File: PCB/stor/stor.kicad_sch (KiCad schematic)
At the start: 45 parts, among them J1 Conn_01x04_Socket, SW1 TS1603-TZ38HBM, SW2 TS1603-TZ38HBM, U1 STM32H723VGT6, U2 TYPE-C 24P-GTJB 040, U3 USB3300-EZK-TR, U4 TPS62177DQCR, X1 25mhz, X2 32.768k, X3 24mhz

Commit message: soo much routing
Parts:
- added R10, R11, R7, R8, R9: 10k, easyeda2kicad:R0402, symbol easyeda2kicad:RC0402FR-0710KL
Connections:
- net PC10: now also R10.2
- net PC11: now also R11.2
- net PC12: now also U1.80 (PC12)
- net PC8: now also R7.1
- net PC9: now also R8.1
- net PD2: now also R9.2
- net VDD: now also R10.1, R11.1, R7.2, R8.2, R9.1

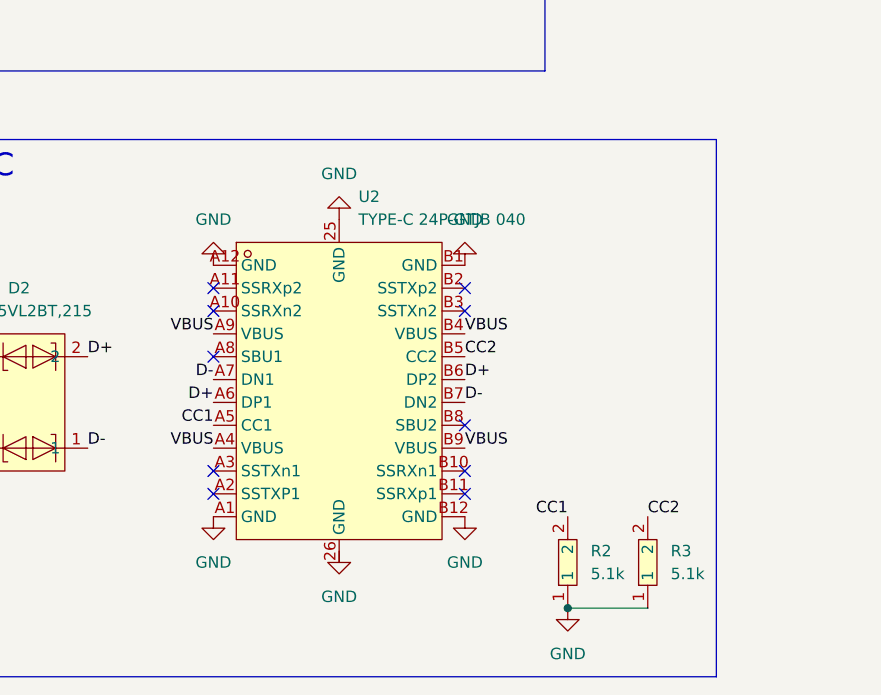
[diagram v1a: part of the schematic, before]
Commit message: new usb and uh finish routing!
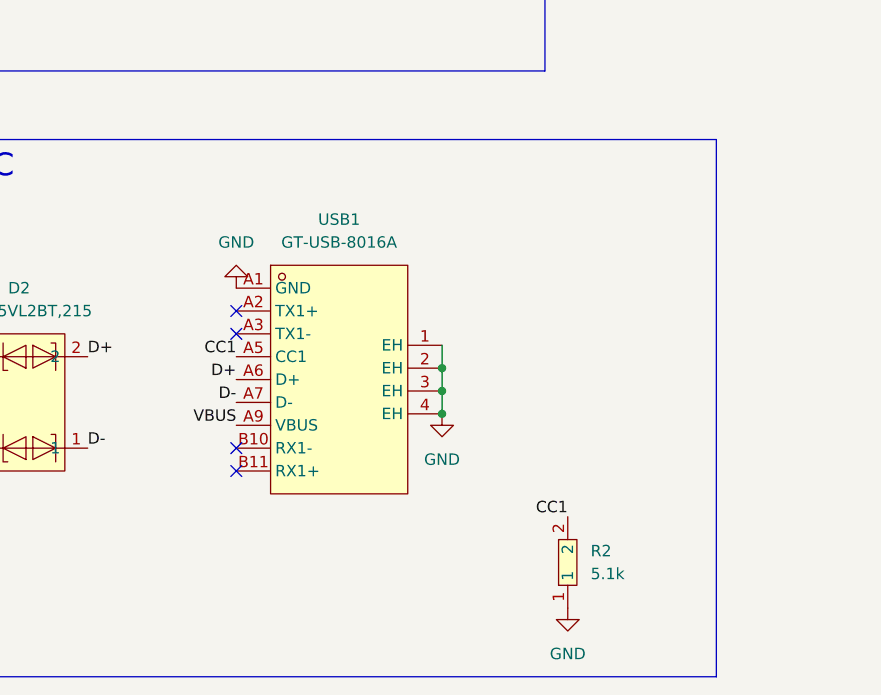
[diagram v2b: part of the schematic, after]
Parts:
- removed R3: 5.1k, easyeda2kicad:R0402, symbol easyeda2kicad:RC0402FR-075K1L
- removed U2: TYPE-C 24P-GTJB 040, easyeda2kicad:USB-C-SMD_TYPE-C-24P-GTJB-040, symbol easyeda2kicad:TYPE-C24P-GTJB040
- added USB1: GT-USB-8016A, easyeda2kicad:USB-TYPE-C-SMD_GT-USB-8016A, symbol easyeda2kicad:GT-USB-8016A
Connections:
- net CC1: now also USB1.A5 (CC1)
- net D+: now also USB1.A6 (D+)
- net D-: now also USB1.A7 (D-)
- net GND: now also USB1.1 (EH), USB1.2 (EH), USB1.3 (EH), USB1.4 (EH), USB1.A1 (GND)
- net VBUS: now also USB1.A9 (VBUS)
- no-connect marks 14 -> 8

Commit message: Reapply "um"
This reverts commit 07b64e62ca9c6bf6512e2ad29080b55d79604863.
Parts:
- removed C11, C12: 10pF, easyeda2kicad:C0402, symbol easyeda2kicad:CC0402JRNPO9BN100
- removed C13, C14: 12pF, easyeda2kicad:C0402, symbol easyeda2kicad:CC0402JRNPO9BN120
- removed C17: 22uF, easyeda2kicad:C0402, symbol easyeda2kicad:GRM158C80G226ME01D
- removed C18: 4.7uF, easyeda2kicad:C0402, symbol easyeda2kicad:CL05A475KP5NRNC
- removed C24, C25: 33pF, easyeda2kicad:C0402, symbol easyeda2kicad:CL05C330JB5NNNC
- removed D2: PESD15VL2BT,215, easyeda2kicad:SOT-23-3_L2.9-W1.3-P1.90-LS2.4-BR, symbol easyeda2kicad:PESD15VL2BT,215
- added C11, C12, C13, C14, C24, C25: 18pF, easyeda2kicad:C0402, symbol lcsc:CC0402JRNPO9BN180
- added C17: 22uF, easyeda2kicad:C0402, symbol lcsc:HGC0402R5226M100NTEJ
- added C18, C27: 100nF, easyeda2kicad:C0402, symbol easyeda2kicad:CC0402KRX7R7BB104
- added C29: 4.7uF, easyeda2kicad:C0402, symbol easyeda2kicad:CL05A475KP5NRNC
- added D1: USBLC6-2SC6, easyeda2kicad:SOT-23-6_L2.9-W1.6-P0.95-LS2.8-BL, symbol lcsc:USBLC6-2SC6
- R6: value 1mΩ -> 1 MΩ
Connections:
- net D+: now also D1.3, D1.4
- net D-: now also D1.1, D1.6
- net GND: now also C11.2, C12.2, C13.2, C14.2, C17.1, C18.1, C24.1, C25.1, C27.1, C29.2, D1.2
- net PC14: now also C13.1
- net PC15: now also C14.1
- net PH0: now also C12.1
- net PH1: now also C11.1
- net VBUS: now also D1.5
- net VDD: now also C21.2, U4.8 (SLEEP), C17.2, C18.2, C27.2, C29.1
- net XI: now also C25.2
- net XO: now also C24.2
- net VDD1.8: now reaches C19.2, U3.15 (VDD1.8)
- net VDD1.8: now also C20.2, U3.26 (VDD1.8)
- no-connect marks 8 -> 7
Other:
- moved on the sheet: R2, USB1

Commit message: zomg
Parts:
- removed J1: Conn_01x04_Socket, Connector_PinHeader_2.54mm:PinHeader_1x04_P2.54mm_Vertical, symbol Connector:Conn_01x04_Socket
- added J1: Conn_01x05_Socket, Connector_PinSocket_2.54mm:PinSocket_1x05_P2.54mm_Vertical, symbol Connector:Conn_01x05_Socket
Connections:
- net GND: now also J1.1 (Pin_1)
- net NRST: now also J1.2 (Pin_2)
- net SWCLK: now also J1.3 (Pin_3)
- net SWDIO: now also J1.4 (Pin_4)
- net VDD: now also J1.5 (Pin_5)
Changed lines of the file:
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@@
 		)
 	)
-	(label "XO"
-		(at 229.87 33.02 180)
+	(label "NRST"
+		(at 24.13 106.68 0)
 		(effects
 			(font
 				(size 1.27 1.27)
 			)
-			(justify right bottom)
+			(justify left bottom)
 		)
 	)
 	(label "XO"
-		(at 251.46 29.21 180)
+		(at 229.87 33.02 180)
 		(effects
 			(font
@@
 		)
 	)
-	(label "SWDIO"
-		(at 35.56 90.17 0)
+	(label "XO"
+		(at 251.46 29.21 180)
 		(effects
 			(font
 				(size 1.27 1.27)
 			)
-			(justify left bottom)
+			(justify right bottom)
 		)
 	)
@@
 		)
 	)
-	(label "VDD"
-		(at 35.56 87.63 0)
-		(effects
-			(font
-				(size 1.27 1.27)
-			)
-			(justify left bottom)
-		)
-	)
 	(label "PB0"
 		(at 251.46 73.66 0)
@@
 		)
 	)
+	(label "SWCLK"
+		(at 24.13 104.14 0)
+		(effects
+			(font
+				(size 1.27 1.27)
+			)
+			(justify left bottom)
+		)
+	)
 	(label "VDD"
 		(at 100.33 189.23 0)
@@
 		)
 	)
+	(label "SWDIO"
+		(at 24.13 101.6 0)
+		(effects
+			(font
+				(size 1.27 1.27)
+			)
+			(justify left bottom)
+		)
+	)
 	(label "PC8"
 		(at 284.48 38.1 180)
@@
 		)
 	)
-	(label "SWCLK"
-		(at 35.56 92.71 0)
-		(effects
-			(font
-				(size 1.27 1.27)
-			)
-			(justify left bottom)
-		)
-	)
 	(label "VDD"
 		(at 191.77 106.68 180)
@@
 		)
 	)
+	(label "VDD"
+		(at 24.13 99.06 0)
+		(effects
+			(font
+				(size 1.27 1.27)
+			)
+			(justify left bottom)
+		)
+	)
 	(label "PC15"
 		(at 116.84 43.18 180)
@@
 	(symbol
 		(lib_id "power:GND")
+		(at 24.13 109.22 0)
+		(unit 1)
+		(body_style 1)
+		(exclude_from_sim no)
+		(in_bom yes)
+		(on_board yes)
+		(in_pos_files yes)
+		(dnp no)
+		(property "Reference" "#PWR020"
+			(at 24.13 115.57 0)
+			(hide yes)
+			(show_name no)
+			(do_not_autoplace no)
+			(effects
+				(font
+					(size 1.27 1.27)
+				)
+			)
+		)
+		(property "Value" "GND"
+			(at 22.86 113.284 0)
+			(show_name no)
+			(do_not_autoplace no)
+			(effects
+				(font
+					(size 1.27 1.27)
+				)
+			)
+		)
+		(property "Footprint" ""
+			(at 24.13 109.22 0)
+			(hide yes)
+			(show_name no)
+			(do_not_autoplace no)
+			(effects
+				(font
+					(size 1.27 1.27)
+				)
+			)
+		)
+		(property "Datasheet" ""
+			(at 24.13 109.22 0)
+			(hide yes)
+			(show_name no)
+			(do_not_autoplace no)
+			(effects
+				(font
+					(size 1.27 1.27)
+				)
+			)
+		)
+		(property "Description" "Power symbol creates a global label with name \"GND\" , ground"
+			(at 24.13 109.22 0)
+			(hide yes)
+			(show_name no)
+			(do_not_autoplace no)
+			(effects
+				(font
+					(size 1.27 1.27)
+				)
+			)
+		)
+		(pin "1"
+		)
+		(instances
+			(project "stor"
+				(path "/d0bb07ec-2650-48b2-bcd0-488070624271"
+					(reference "#PWR020")
+					(unit 1)
+				)
+			)
+		)
+	)
+	(symbol
+		(lib_id "power:GND")
 		(at 158.75 199.39 90)
 		(unit 1)
@@
 	)
 	(symbol
-		(lib_id "Connector:Conn_01x04_Socket")
-		(at 30.48 92.71 180)
-		(unit 1)
-		(body_style 1)
-		(exclude_from_sim no)
-		(in_bom yes)
-		(on_board yes)
-		(in_pos_files yes)
-		(dnp yes)
-		(fields_autoplaced yes)
-		(property "Reference" "J1"
-			(at 31.115 82.55 0)
-			(show_name no)
-			(do_not_autoplace no)
-			(effects
-				(font
-					(size 1.27 1.27)
-				)
-			)
-		)
-		(property "Value" "Conn_01x04_Socket"
-			(at 31.115 85.09 0)
-			(show_name no)
-			(do_not_autoplace no)
-			(effects
-				(font
-					(size 1.27 1.27)
-				)
-			)
-		)
-		(property "Footprint" "Connector_PinHeader_2.54mm:PinHeader_1x04_P2.54mm_Vertical"
-			(at 30.48 92.71 0)
-			(hide yes)
-			(show_name no)
-			(do_not_autoplace no)
-			(effects
-				(font
-					(size 1.27 1.27)
-				)
-			)
-		)
-		(property "Datasheet" ""
-			(at 30.48 92.71 0)
-			(hide yes)
-			(show_name no)
-			(do_not_autoplace no)
-			(effects
-				(font
-					(size 1.27 1.27)
-				)
-			)
-		)
-		(property "Description" "Generic connector, single row, 01x04, script generated"
-			(at 30.48 92.71 0)
-			(hide yes)
-			(show_name no)
-			(do_not_autoplace no)
-			(effects
-				(font
-					(size 1.27 1.27)
-				)
-			)
-		)
-		(pin "3"
-		)
-		(pin "4"
-		)
-		(pin "2"
-		)
-		(pin "1"
-		)
-		(instances
-			(project "stor"
-				(path "/d0bb07ec-2650-48b2-bcd0-488070624271"
-					(reference "J1")
-					(unit 1)
-				)
-			)
-		)
-	)
-	(symbol
 		(lib_id "power:GND")
 		(at 64.77 50.8 270)
@@
 	)
 	(symbol
+		(lib_id "Connector:Conn_01x05_Socket")
+		(at 19.05 104.14 180)
+		(unit 1)
+		(body_style 1)
+		(exclude_from_sim no)
+		(in_bom yes)
+		(on_board yes)
+		(in_pos_files yes)
+		(dnp yes)
+		(fields_autoplaced yes)
+		(property "Reference" "J1"
+			(at 19.685 93.98 0)
+			(show_name no)
+			(do_not_autoplace no)
+			(effects
+				(font
+					(size 1.27 1.27)
+				)
+			)
+		)
+		(property "Value" "Conn_01x05_Socket"
+			(at 19.685 96.52 0)
+			(show_name no)
+			(do_not_autoplace no)
+			(effects
+				(font
+					(size 1.27 1.27)
+				)
+			)
+		)
+		(property "Footprint" "Connector_PinSocket_2.54mm:PinSocket_1x05_P2.54mm_Vertical"
+			(at 19.05 104.14 0)
+			(hide yes)
+			(show_name no)
+			(do_not_autoplace no)
+			(effects
+				(font
+					(size 1.27 1.27)
+				)
+			)
+		)
+		(property "Datasheet" ""
+			(at 19.05 104.14 0)
+			(hide yes)
+			(show_name no)
+			(do_not_autoplace no)
+			(effects
+				(font
+					(size 1.27 1.27)
+				)
+			)
+		)
+		(property "Description" "Generic connector, single row, 01x05, script generated"
+			(at 19.05 104.14 0)
+			(hide yes)
+			(show_name no)
+			(do_not_autoplace no)
+			(effects
+				(font
+					(size 1.27 1.27)
+				)
+			)
+		)
+		(pin "4"
+		)
+		(pin "2"
+		)
+		(pin "3"
+		)
+		(pin "1"
+		)
+		(pin "5"
+		)
+		(instances
+			(project "stor"
+				(path "/d0bb07ec-2650-48b2-bcd0-488070624271"
+					(reference "J1")
+					(unit 1)
+				)
+			)
+		)
+	)
+	(symbol
 		(lib_id "easyeda2kicad:STM32H723VGT6")
 		(at 138.43 85.09 0)
@@
 					(unit 1)
 				)
-			)
-		)
-	)
-	(symbol
-		(lib_id "power:GND")
-		(at 35.56 95.25 0)
-		(unit 1)
-		(body_style 1)
-		(exclude_from_sim no)
-		(in_bom yes)
-		(on_board yes)
-		(in_pos_files yes)
-		(dnp no)
-		(fields_autoplaced yes)
-		(property "Reference" "#PWR07"
-			(at 35.56 101.6 0)
-			(hide yes)
-			(show_name no)
-			(do_not_autoplace no)
-			(effects
-				(font
-					(size 1.27 1.27)
-				)
-			)
-		)
-		(property "Value" "GND"
-			(at 35.56 100.33 0)
-			(show_name no)
-			(do_not_autoplace no)
-			(effects
-				(font
-					(size 1.27 1.27)
-				)
-			)
-		)
-		(property "Footprint" ""
-			(at 35.56 95.25 0)
-			(hide yes)
-			(show_name no)
-			(do_not_autoplace no)
-			(effects
-				(font
-					(size 1.27 1.27)
-				)
-			)
-		)
-		(property "Datasheet" ""
-			(at 35.56 95.25 0)
-			(hide yes)
-			(show_name no)
-			(do_not_autoplace no)
-			(effects
-				(font
-					(size 1.27 1.27)
-				)
-			)
-		)
-		(property "Description" "Power symbol creates a global label with name \"GND\" , ground"
-			(at 35.56 95.25 0)
-			(hide yes)
-			(show_name no)
-			(do_not_autoplace no)
-			(effects
-				(font
-					(size 1.27 1.27)
-				)
-			)
-		)
-		(pin "1"
-		)
-		(instances
-			(project "stor"
-				(path "/d0bb07ec-2650-48b2-bcd0-488070624271"
-					(reference "#PWR07")
-					(unit 1)
-				)

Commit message: pcb
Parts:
- added J2: Conn_01x03_Socket, Connector_PinSocket_2.54mm:PinSocket_1x03_P2.54mm_Vertical, symbol Connector:Conn_01x03_Socket
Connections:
- net GND: now also J2.1 (Pin_1)
- net PA9: now reaches U1.68 (PA9)
- net PA9: now also J2.2 (Pin_2)
- net PA10: now reaches U1.69 (PA10)
- net PA10: now also J2.3 (Pin_3)
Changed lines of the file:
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@@
 		)
 	)
+	(label "PA9"
+		(at 26.67 123.19 0)
+		(effects
+			(font
+				(size 1.27 1.27)
+			)
+			(justify left bottom)
+		)
+	)
 	(label "VDD"
 		(at 223.52 53.34 90)
@@
 		)
 	)
+	(label "PA10"
+		(at 157.48 101.6 0)
+		(effects
+			(font
+				(size 1.27 1.27)
+			)
+			(justify left bottom)
+		)
+	)
 	(label "PD4"
 		(at 157.48 60.96 0)
@@
 		)
 	)
+	(label "PA10"
+		(at 26.67 120.65 0)
+		(effects
+			(font
+				(size 1.27 1.27)
+			)
+			(justify left bottom)
+		)
+	)
 	(label "PC0"
 		(at 228.6 106.68 270)
@@
 		)
 	)
+	(label "PA9"
+		(at 157.48 104.14 0)
+		(effects
+			(font
+				(size 1.27 1.27)
+			)
+			(justify left bottom)
+		)
+	)
 	(label "VDD"
 		(at 116.84 73.66 180)
@@
 	(symbol
 		(lib_id "power:GND")
+		(at 26.67 125.73 0)
+		(unit 1)
+		(body_style 1)
+		(exclude_from_sim no)
+		(in_bom yes)
+		(on_board yes)
+		(in_pos_files yes)
+		(dnp no)
+		(property "Reference" "#PWR021"
+			(at 26.67 132.08 0)
+			(hide yes)
+			(show_name no)
+			(do_not_autoplace no)
+			(effects
+				(font
+					(size 1.27 1.27)
+				)
+			)
+		)
+		(property "Value" "GND"
+			(at 25.4 129.794 0)
+			(show_name no)
+			(do_not_autoplace no)
+			(effects
+				(font
+					(size 1.27 1.27)
+				)
+			)
+		)
+		(property "Footprint" ""
+			(at 26.67 125.73 0)
+			(hide yes)
+			(show_name no)
+			(do_not_autoplace no)
+			(effects
+				(font
+					(size 1.27 1.27)
+				)
+			)
+		)
+		(property "Datasheet" ""
+			(at 26.67 125.73 0)
+			(hide yes)
+			(show_name no)
+			(do_not_autoplace no)
+			(effects
+				(font
+					(size 1.27 1.27)
+				)
+			)
+		)
+		(property "Description" "Power symbol creates a global label with name \"GND\" , ground"
+			(at 26.67 125.73 0)
+			(hide yes)
+			(show_name no)
+			(do_not_autoplace no)
+			(effects
+				(font
+					(size 1.27 1.27)
+				)
+			)
+		)
+		(pin "1"
+		)
+		(instances
+			(project "stor"
+				(path "/d0bb07ec-2650-48b2-bcd0-488070624271"
+					(reference "#PWR021")
+					(unit 1)
+				)
+			)
+		)
+	)
+	(symbol
+		(lib_id "power:GND")
 		(at 264.16 54.61 90)
 		(unit 1)
@@
 					(unit 1)
 				)
+			)
+		)
+	)
+	(symbol
+		(lib_id "Connector:Conn_01x03_Socket")
+		(at 21.59 123.19 180)
+		(unit 1)
+		(body_style 1)
+		(exclude_from_sim no)
+		(in_bom yes)
+		(on_board yes)
+		(in_pos_files yes)
+		(dnp yes)
+		(fields_autoplaced yes)
+		(property "Reference" "J2"
+			(at 22.225 115.57 0)
+			(show_name no)
+			(do_not_autoplace no)
+			(effects
+				(font
+					(size 1.27 1.27)
+				)
+			)
+		)
+		(property "Value" "Conn_01x03_Socket"
+			(at 22.225 118.11 0)
+			(show_name no)
+			(do_not_autoplace no)
+			(effects
+				(font
+					(size 1.27 1.27)
+				)
+			)
+		)
+		(property "Footprint" "Connector_PinSocket_2.54mm:PinSocket_1x03_P2.54mm_Vertical"
+			(at 21.59 123.19 0)
+			(hide yes)
+			(show_name no)
+			(do_not_autoplace no)
+			(effects
+				(font
+					(size 1.27 1.27)
+				)
+			)
+		)
+		(property "Datasheet" ""
+			(at 21.59 123.19 0)
+			(hide yes)
+			(show_name no)
+			(do_not_autoplace no)
+			(effects
+				(font
+					(size 1.27 1.27)
+				)
+			)
+		)
+		(property "Description" "Generic connector, single row, 01x03, script generated"
+			(at 21.59 123.19 0)
+			(hide yes)
+			(show_name no)
+			(do_not_autoplace no)
+			(effects
+				(font
+					(size 1.27 1.27)
+				)
+			)
+		)
+		(pin "3"
+		)
+		(pin "1"
+		)
+		(pin "2"
+		)
+		(instances
+			(project "stor"
+				(path "/d0bb07ec-2650-48b2-bcd0-488070624271"
+					(reference "J2")
+					(unit 1)
+				)

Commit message: firmware and LEDs lol
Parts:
- removed J2: Conn_01x03_Socket, Connector_PinSocket_2.54mm:PinSocket_1x03_P2.54mm_Vertical, symbol Connector:Conn_01x03_Socket
- added J2: Conn_01x04_Socket, Connector_PinSocket_2.54mm:PinSocket_1x04_P2.54mm_Vertical, symbol Connector:Conn_01x04_Socket
- added LED1: KT-0603R, easyeda2kicad:LED-SMD_L1.6-W0.8-R-RD, symbol lcsc:KT-0603R
- added LED2: 0603White light_C2290, easyeda2kicad:LED0603-R-RD_WHITE, symbol lcsc:0603Whitelight_C2290
- added R12: 220Ω, easyeda2kicad:R0402, symbol lcsc:0402WGF2200TCE
- added R3: 1kΩ, easyeda2kicad:R0402, symbol lcsc:0402WGF1001TCE
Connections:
- net GND: now also J2.1 (Pin_1), LED1.2 (K), LED2.2 (K)
- net PA10: now also J2.4 (Pin_4)
- net PA9: now also J2.3 (Pin_3)
- net VDD: now also J2.2 (Pin_2)
- net PA6: now reaches U1.30 (PA6)
- net PA6: now also R12.2
- net PA7: now reaches U1.31 (PA7)
- net PA7: now also R3.2
- new net: LED2.1 (A), R12.1
- new net: LED1.1 (A), R3.1
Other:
- note added: "red"
- note added: "white"

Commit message: new usb
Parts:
- removed C17: 22uF, easyeda2kicad:C0402, symbol lcsc:HGC0402R5226M100NTEJ
- removed R2: 5.1k, easyeda2kicad:R0402, symbol easyeda2kicad:RC0402FR-075K1L
- removed USB1: GT-USB-8016A, easyeda2kicad:USB-TYPE-C-SMD_GT-USB-8016A, symbol easyeda2kicad:GT-USB-8016A
- added C17: 22uF, easyeda2kicad:C0603, symbol lcsc:CL10A226MQ8NRNC
- added USB1: U-USBAR04P-M001, easyeda2kicad:USB-SMD_KH-USB-AM-4P-CB, symbol lcsc:U-USBAR04P-M001
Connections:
- net D+: now also USB1.3 (D+)
- net D-: now also USB1.2 (D-)
- net GND: now also C17.1, USB1.4 (GND), USB1.5 (EH), USB1.6 (EH)
- net VBUS: now also USB1.1 (VCC)
- net VDD: now also C17.2
- no-connect marks 7 -> 3

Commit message: bom opt!!
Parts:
- C1, C16, C2: symbol easyeda2kicad:CL05A225KO5NQNC -> easyeda2kicad:CL05A225MQ5NSNC; LCSC Part C170151 -> C12530; MPN CL05A225KO5NQNC -> CL05A225MQ5NSNC; Manufacturer SAMSUNG(三星) -> Samsung Electro-Mechanics
- C10, C15, C18, C19, C21, C23, C26, C27, C3, C4, C5, C6, C7, C8, C9: symbol easyeda2kicad:CC0402KRX7R7BB104 -> easyeda2kicad:CL05B104KO5NNNC; LCSC Part C60474 -> C1525; MPN CC0402KRX7R7BB104 -> CL05B104KO5NNNC; Manufacturer YAGEO(国巨) -> Samsung Electro-Mechanics
- C11, C12, C13, C14, C24, C25: symbol lcsc:CC0402JRNPO9BN180 -> lcsc:0402CG180J500NT; LCSC Part C106202 -> C1549; MPN CC0402JRNPO9BN180 -> 0402CG180J500NT; Manufacturer YAGEO(国巨) -> FH
- C20, C22, C29: symbol easyeda2kicad:CL05A475KP5NRNC -> easyeda2kicad:CL05A475MP5NRNC; LCSC Part C368809 -> C23733; MPN CL05A475KP5NRNC -> CL05A475MP5NRNC; Manufacturer SAMSUNG(三星) -> Samsung Electro-Mechanics
- J1, J2: now left out of the parts list
- R1, R10, R11, R7, R8, R9: symbol easyeda2kicad:RC0402FR-0710KL -> easyeda2kicad:0402WGF1002TCE; LCSC Part C60490 -> C25744; MPN RC0402FR-0710KL -> 0402WGF1002TCE; Manufacturer YAGEO(国巨) -> UNI-ROYAL
- R4: symbol easyeda2kicad:RC0402FR-07100KL -> easyeda2kicad:0402WGF1003TCE; LCSC Part C60491 -> C25741; MPN RC0402FR-07100KL -> 0402WGF1003TCE; Manufacturer YAGEO(国巨) -> UNI-ROYAL
- R5: symbol easyeda2kicad:RC0402FR-0712KL -> easyeda2kicad:0402WGF1202TCE; LCSC Part C114760 -> C25752; MPN RC0402FR-0712KL -> 0402WGF1202TCE; Manufacturer YAGEO(国巨) -> UNI-ROYAL
- R6: symbol easyeda2kicad:RC0402FR-071ML -> easyeda2kicad:0402WGF1004TCE; LCSC Part C138033 -> C26083; MPN RC0402FR-071ML -> 0402WGF1004TCE; Manufacturer YAGEO(国巨) -> UNI-ROYAL
